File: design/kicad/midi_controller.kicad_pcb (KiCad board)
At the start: 2 copper layers, 166 x 166 mm, 26 parts, among them J1 Conn_01x02_Socket, J2 Conn_01x02_Socket, J3 Conn_01x02_Socket, J4 Conn_01x02_Socket, J5 Conn_01x02_Socket, J6 Conn_01x02_Socket, J7 Conn_01x05, SW1 MIDI_Switch_Pushbutton_PV0H24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, SW2 MIDI_Switch_Pushbutton_PV0H24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, SW3 MIDI_Switch_Pushbutton_PV0H24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, SW4 MIDI_Switch_Pushbutton_PV0H24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, SW5 MIDI_Switch_Pushbutton_PV0H24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, SW6 MIDI_Switch_Pushbutton_PV0H24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, U1 CD74HC4067M

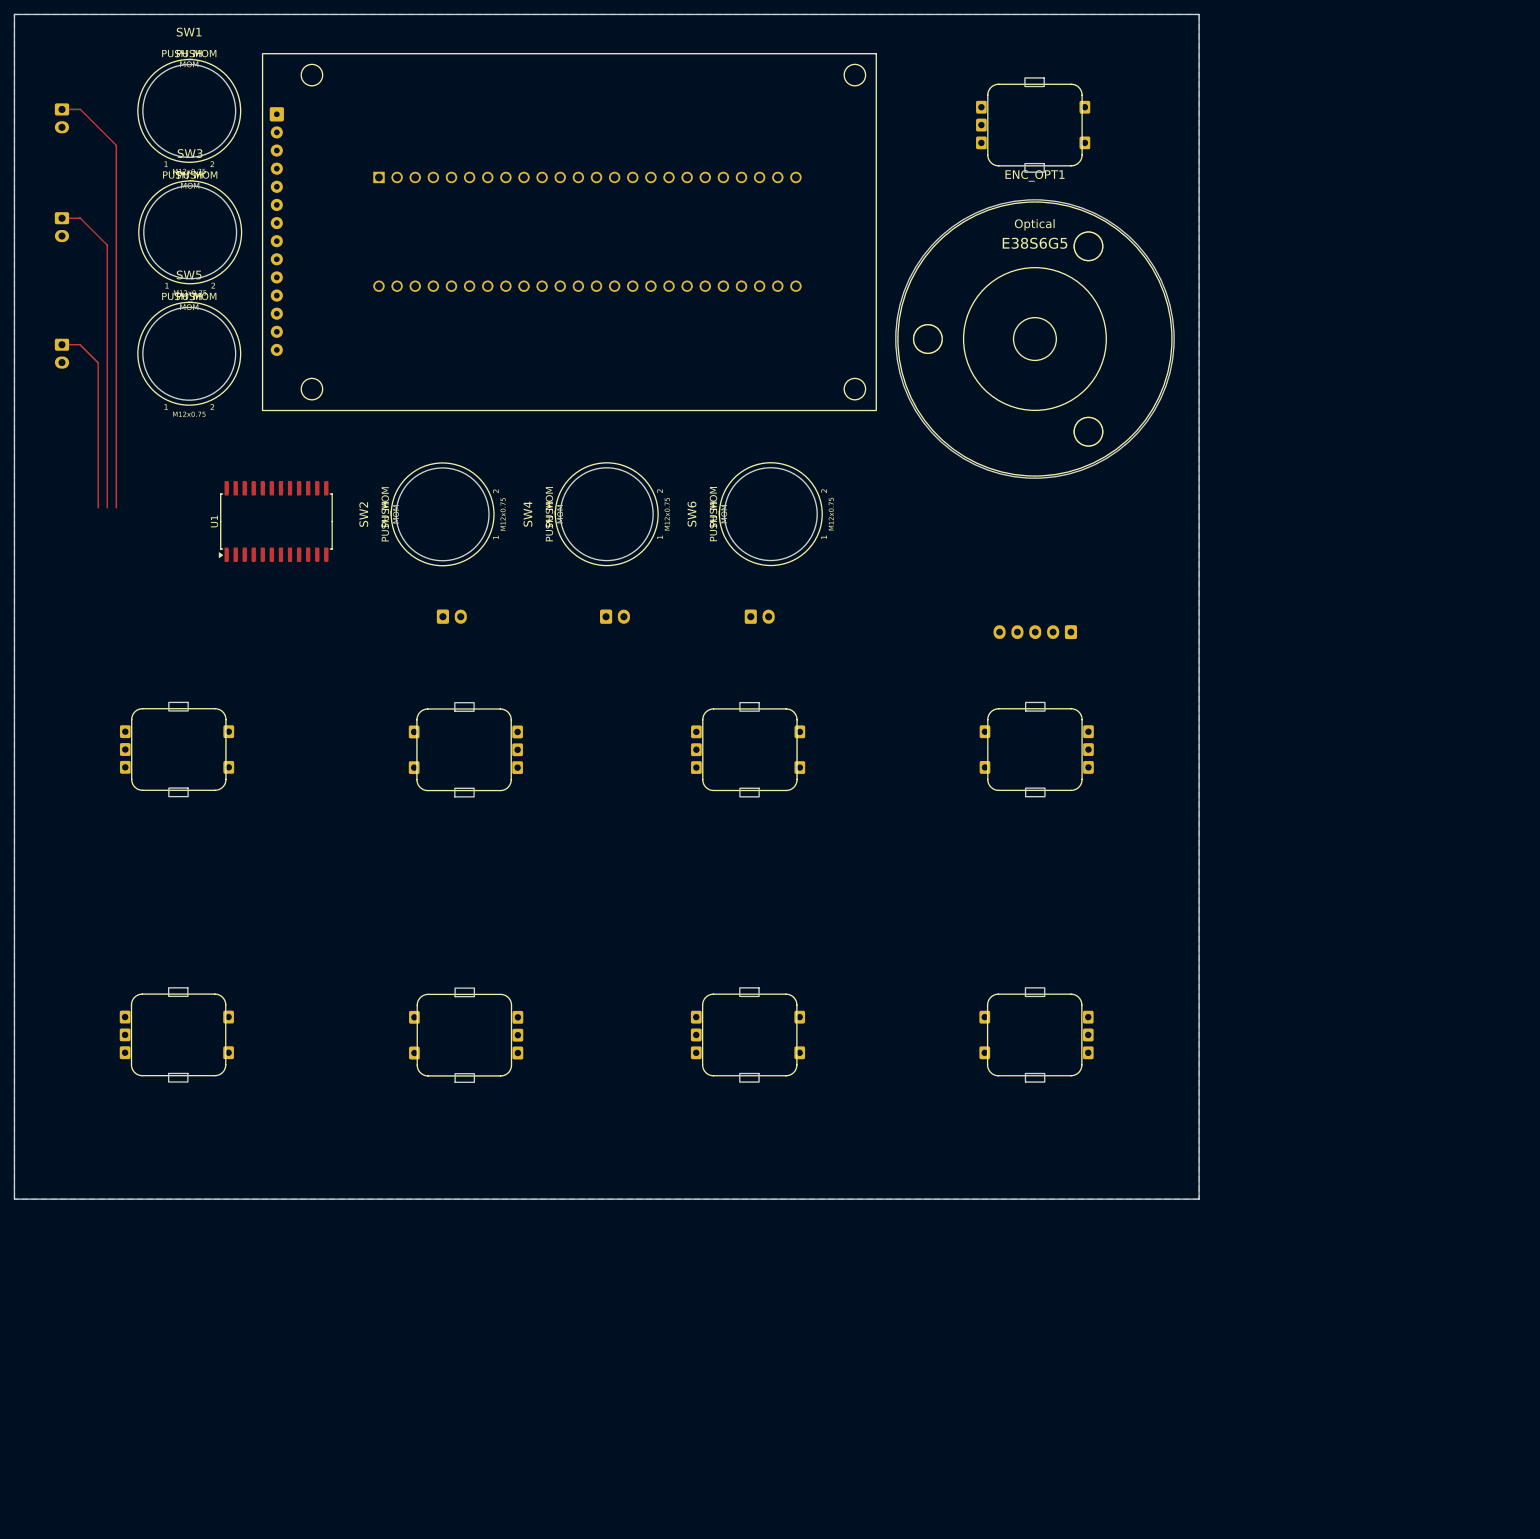
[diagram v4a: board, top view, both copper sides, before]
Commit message: Update kicad binary files
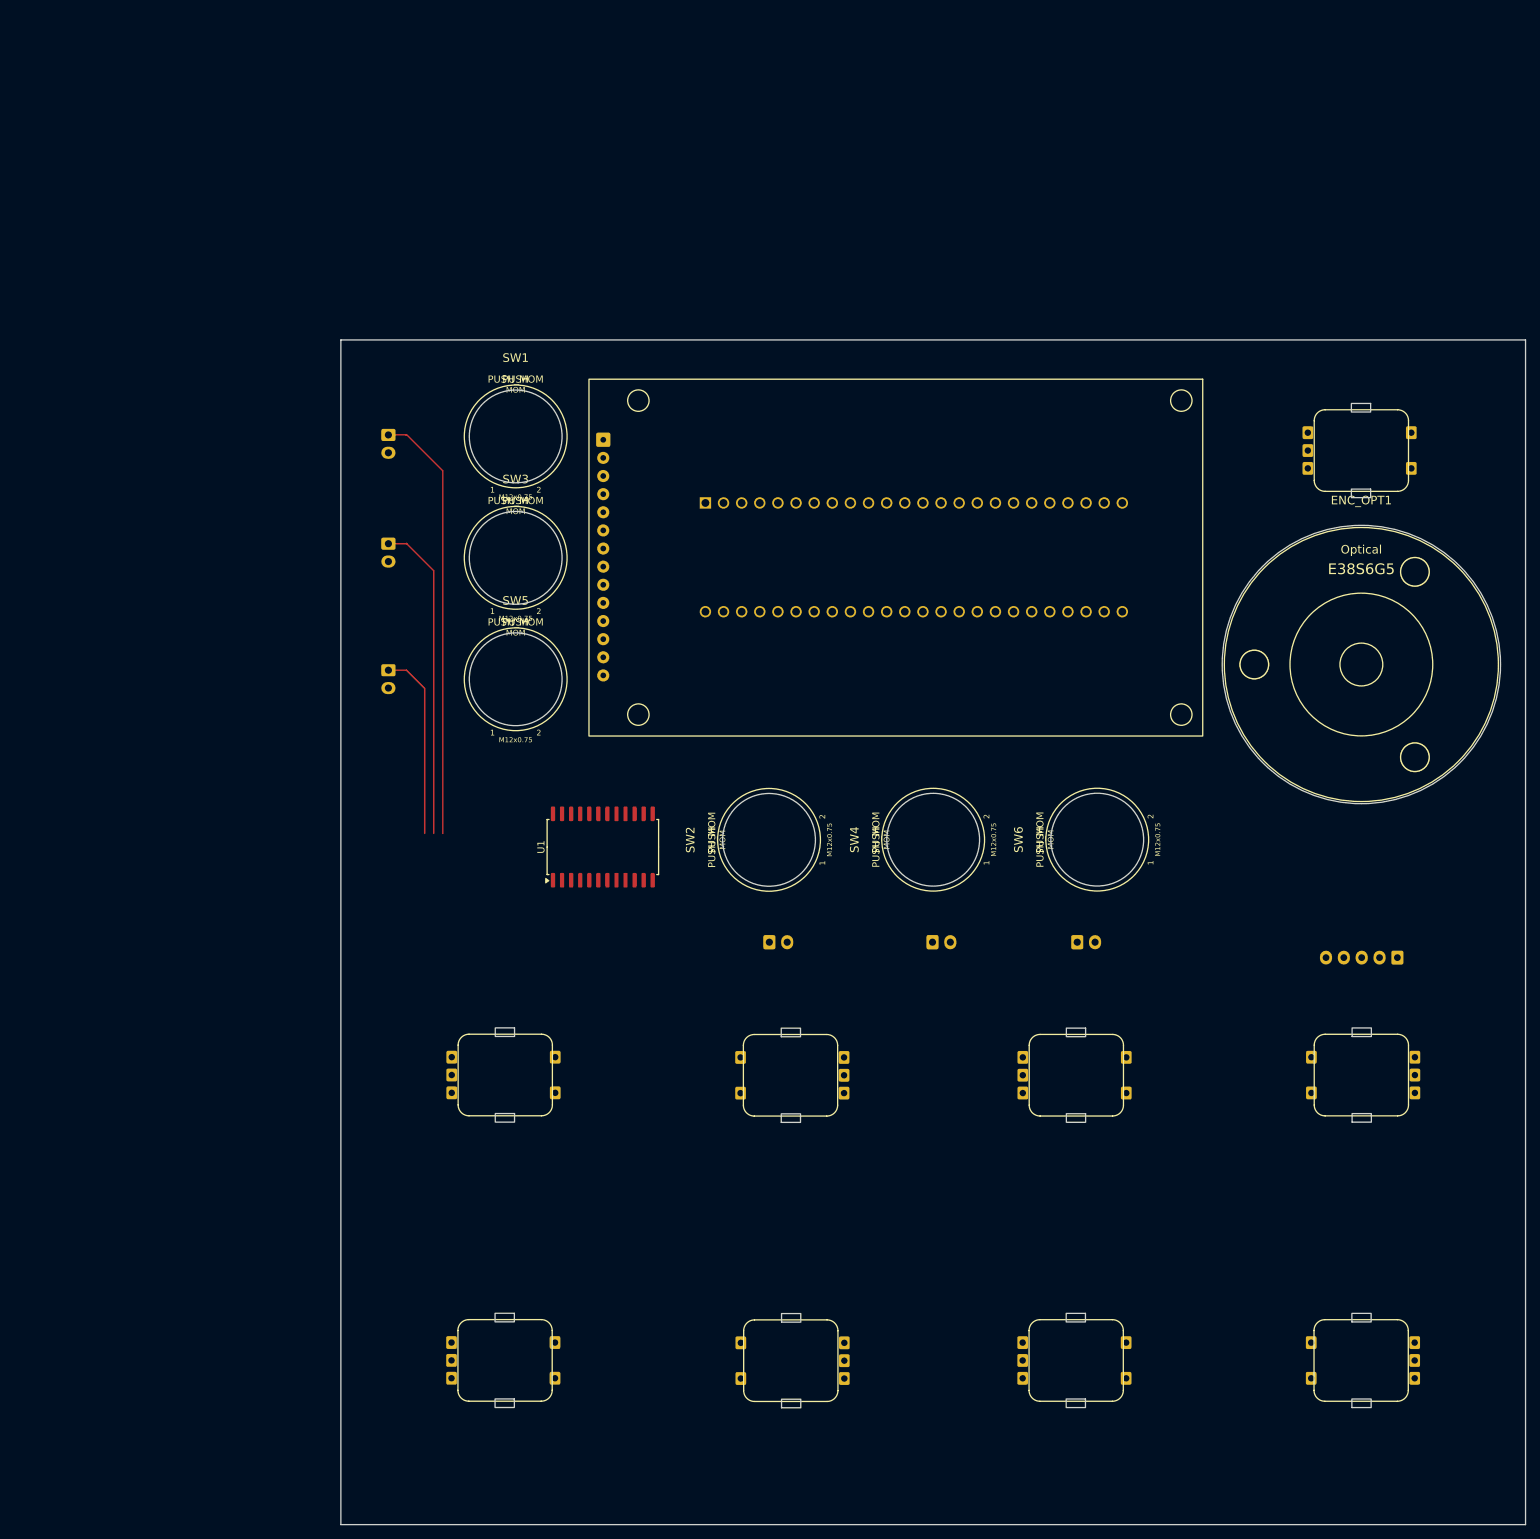
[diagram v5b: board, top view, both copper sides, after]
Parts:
- moved ENC_MECH1 64.6 mm to (100.0, 180.0)
- moved ENC_MECH3 64.6 mm to (180.1, 180.0)
- moved ENC_MECH6 64.6 mm to (140.1, 220.0)
- moved ENC_MECH8 64.6 mm to (220.0, 220.0)
- moved J2 64.6 mm to (83.7, 105.6)
- moved J4 64.6 mm to (180.2, 161.4)
- moved J5 64.6 mm to (159.9, 161.4)
- moved J6 64.6 mm to (137.0, 161.4)
- moved J7 64.6 mm to (225.0, 163.6)
- moved MCU1 64.6 mm to (157.3, 107.5)
- moved D1 64.6 mm to (113.8, 107.5)
- moved ENC_MECH4 64.6 mm to (220.0, 180.0)
- moved ENC_MECH5 64.6 mm to (100.0, 220.0)
- moved ENC_MECH7 64.6 mm to (180.0, 220.0)
- moved ENC_MECH9 64.6 mm to (220.0, 92.5)
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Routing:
- added copper zone on In1.Cu, net /Buttons_Momentary/GND
- removed copper zone on B.Cu, net /Buttons_Momentary/GND
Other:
- copper layers 2 -> 4
- board text removed: "-"
- board text removed: "----"
- board text removed: "1"
- board text removed: "1 of 1"
- board text removed: "10"
- board text removed: "1:1"
- board text removed: "2"
- board text removed: "2025-07-25"
- board text removed: "3"
- board text removed: "4"
- board text removed: "5"
- board text removed: "6"
- board text removed: "7"
- board text removed: "8"
- board text removed: "9"
- board text removed: "A"
- board text removed: "APPROVED"
- board text removed: "B"
- board text removed: "BODY"
- board text removed: "BREAK ALL SHARP EDGES AND REMOVE BURRS"
- board text removed: "C"
- board text removed: "CHECKED"
- board text removed: "D"
- board text removed: "DATE"
- board text removed: "DO NOT SCALE DRAWING"
- board text removed: "DRAWN"
- board text removed: "DWG NO."
- board text removed: "Description"
- board text removed: "ENCODER_OPTICAL_E38S6G5"
- board text removed: "FINISH"
- board text removed: "FIRST ANGLE PROJECTION"
- board text removed: "Item"
- board text removed: "KNOB"
- board text removed: "MATERIAL"
- board text removed: "NAME"
- board text removed: "Name"
- board text removed: "PEC11R_4220F_S0024"
- board text removed: "PLATE_BOTTOM"
- board text removed: "PLATE_FRONT_METAL"
- board text removed: "PUSH_BUTTON"
- board text removed: "Part number"
- board text removed: "Quantity"
- board text removed: "REV."
- board text removed: "SCALE"
- board text removed: "SCREEN"
- board text removed: "SHEET"
- board text removed: "SIGNATURE"
- board text removed: "SIMON BRUN"
- board text removed: "SIZE"
- board text removed: "SURFACE FINISH"
- board text removed: "TITLE"
- board text removed: "UNLESS OTHERWISE SPECIFIED, DIMENSIONS ARE IN MILLIMETERS"
- board text removed: "WEIGHT"

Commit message: Fix hardware pin configuration and rotary encoder parameters
- Updated CS_PIN from 30 to 28 in SystemConstants.hpp to reflect the correct hardware setup for ILI9341.
- Modified rotary encoder parameters in ConfigurationFactory.cpp, changing the first parameter of asRotaryEncoder from 28 to 23 for proper functionality.
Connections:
- net Net-(J7-Pin_2) renamed ENC_A_NAV
- net Net-(J7-Pin_3) renamed ENC_B_NAV
- D1 pad 1: Net-(D1-VCC) -> +5V
- D1 pad 10: Net-(D1-T_CLK) -> unconnected-(D1-T_CLK-Pad10)
- D1 pad 11: Net-(D1-T_CS) -> unconnected-(D1-T_CS-Pad11)
- D1 pad 12: Net-(D1-T_DIN) -> unconnected-(D1-T_DIN-Pad12)
- D1 pad 13: Net-(D1-T_DO) -> unconnected-(D1-T_DO-Pad13)
- D1 pad 14: Net-(D1-T_IRQ) -> unconnected-(D1-T_IRQ-Pad14)
- D1 pad 2: /Buttons_Momentary/GND -> GND
- D1 pad 8: Net-(D1-LED) -> +3V3
- ENC_MECH1 pad 2: /Buttons_Momentary/GND -> GND
- ENC_MECH1 pad A: /MIDI_Encoder_Matrix_2x4_with_push_buttons/1x1.QUAD_A -> /MIDI_Encoder_Matrix_2x4_with_push_buttons/1x1.QUAD_B
- ENC_MECH1 pad B: /MIDI_Encoder_Matrix_2x4_with_push_buttons/1x1.QUAD_A -> /MIDI_Encoder_Matrix_2x4_with_push_buttons/1x1.QUAD_B
- ENC_MECH1 pad C: /Buttons_Momentary/GND -> GND
- ENC_MECH2 pad 2: /Buttons_Momentary/GND -> GND
- ENC_MECH2 pad A: /MIDI_Encoder_Matrix_2x4_with_push_buttons/1x2.QUAD_A -> /MIDI_Encoder_Matrix_2x4_with_push_buttons/1x2.QUAD_B
- ENC_MECH2 pad B: /MIDI_Encoder_Matrix_2x4_with_push_buttons/1x2.QUAD_A -> /MIDI_Encoder_Matrix_2x4_with_push_buttons/1x2.QUAD_B
- ENC_MECH2 pad C: /Buttons_Momentary/GND -> GND
- ENC_MECH3 pad 2: /Buttons_Momentary/GND -> GND
- ENC_MECH3 pad A: /MIDI_Encoder_Matrix_2x4_with_push_buttons/1x3.QUAD_A -> /MIDI_Encoder_Matrix_2x4_with_push_buttons/1x3.QUAD_B
- ENC_MECH3 pad B: /MIDI_Encoder_Matrix_2x4_with_push_buttons/1x3.QUAD_A -> /MIDI_Encoder_Matrix_2x4_with_push_buttons/1x3.QUAD_B
- ENC_MECH3 pad C: /Buttons_Momentary/GND -> GND
- ENC_MECH4 pad 2: /Buttons_Momentary/GND -> GND
- ENC_MECH4 pad A: /MIDI_Encoder_Matrix_2x4_with_push_buttons/1x4.QUAD_A -> /MIDI_Encoder_Matrix_2x4_with_push_buttons/1x4.QUAD_B
- ENC_MECH4 pad B: /MIDI_Encoder_Matrix_2x4_with_push_buttons/1x4.QUAD_A -> /MIDI_Encoder_Matrix_2x4_with_push_buttons/1x4.QUAD_B
- ENC_MECH4 pad C: /Buttons_Momentary/GND -> GND
- ENC_MECH5 pad 2: /Buttons_Momentary/GND -> GND
- ENC_MECH5 pad A: /MIDI_Encoder_Matrix_2x4_with_push_buttons/2x1.QUAD_A -> /MIDI_Encoder_Matrix_2x4_with_push_buttons/2x1.QUAD_B
- ENC_MECH5 pad B: /MIDI_Encoder_Matrix_2x4_with_push_buttons/2x1.QUAD_A -> /MIDI_Encoder_Matrix_2x4_with_push_buttons/2x1.QUAD_B
- ENC_MECH5 pad C: /Buttons_Momentary/GND -> GND
- ENC_MECH6 pad 2: /Buttons_Momentary/GND -> GND
- ENC_MECH6 pad A: /MIDI_Encoder_Matrix_2x4_with_push_buttons/2x2.QUAD_A -> /MIDI_Encoder_Matrix_2x4_with_push_buttons/2x2.QUAD_B
- ENC_MECH6 pad B: /MIDI_Encoder_Matrix_2x4_with_push_buttons/2x2.QUAD_A -> /MIDI_Encoder_Matrix_2x4_with_push_buttons/2x2.QUAD_B
- ENC_MECH6 pad C: /Buttons_Momentary/GND -> GND
- ENC_MECH7 pad 2: /Buttons_Momentary/GND -> GND
- ENC_MECH7 pad A: /MIDI_Encoder_Matrix_2x4_with_push_buttons/2x3.QUAD_A -> /MIDI_Encoder_Matrix_2x4_with_push_buttons/2x3.QUAD_B
- ENC_MECH7 pad B: /MIDI_Encoder_Matrix_2x4_with_push_buttons/2x3.QUAD_A -> /MIDI_Encoder_Matrix_2x4_with_push_buttons/2x3.QUAD_B
- ENC_MECH7 pad C: /Buttons_Momentary/GND -> GND
- ENC_MECH8 pad 2: /Buttons_Momentary/GND -> GND
- ENC_MECH8 pad A: /MIDI_Encoder_Matrix_2x4_with_push_buttons/2x4.QUAD_A -> /MIDI_Encoder_Matrix_2x4_with_push_buttons/2x4.QUAD_B
- ENC_MECH8 pad B: /MIDI_Encoder_Matrix_2x4_with_push_buttons/2x4.QUAD_A -> /MIDI_Encoder_Matrix_2x4_with_push_buttons/2x4.QUAD_B
- ENC_MECH8 pad C: /Buttons_Momentary/GND -> GND
- ENC_MECH9 pad 2: /Buttons_Momentary/GND -> GND
- ENC_MECH9 pad C: /Buttons_Momentary/GND -> GND
- J1 pad 2: /Buttons_Momentary/GND -> GND
- J2 pad 2: /Buttons_Momentary/GND -> GND
- J3 pad 2: /Buttons_Momentary/GND -> GND
- J4 pad 2: /Buttons_Momentary/GND -> GND
- J5 pad 2: /Buttons_Momentary/GND -> GND
- J6 pad 2: /Buttons_Momentary/GND -> GND
- J7 pad 1: Net-(J7-Pin_1) -> +5V
- J7 pad 4: /Buttons_Momentary/GND -> GND
- J7 pad 5: /Buttons_Momentary/GND -> GND
- MCU1 pad 1: /Buttons_Momentary/GND -> GND
- MCU1 pad 10: Net-(D1-LED) -> unconnected-(MCU1-8_TX2_IN1-Pad10)
- MCU1 pad 11: Net-(D1-RST) -> unconnected-(MCU1-9_OUT1C-Pad11)
- MCU1 pad 12: Net-(D1-CS) -> unconnected-(MCU1-10_CS_MQSR-Pad12)
- MCU1 pad 13: Net-(D1-SDI/MOSI) -> unconnected-(MCU1-11_MOSI_CTX1-Pad13)
- MCU1 pad 14: Net-(D1-SDO/MISO) -> unconnected-(MCU1-12_MISO_MQSL-Pad14)
- MCU1 pad 15: Net-(D1-VCC) -> +3V3
- MCU1 pad 16: Net-(D1-T_IRQ) -> unconnected-(MCU1-24_A10_TX6_SCL2-Pad16)
- MCU1 pad 18: Net-(D1-T_DIN) -> Net-(D1-SDI/MOSI)
- MCU1 pad 19: Net-(D1-T_CLK) -> Net-(D1-SCK)
- MCU1 pad 2: unconnected-(MCU1-0_RX1_CRX2_CS1-Pad2) -> Net-(D1-DC)
- MCU1 pad 20: Net-(D1-T_CS) -> Net-(D1-CS)
- MCU1 pad 21: /Encoder with Push Button_Navigation/QUAD_A -> Net-(D1-RST)
- MCU1 pad 22: /Encoder with Push Button_Navigation/QUAD_B -> unconnected-(MCU1-30_CRX3-Pad22)
- MCU1 pad 27: /MIDI_Encoder_Matrix_2x4_with_push_buttons/1x1.QUAD_A -> unconnected-(MCU1-35_TX8-Pad27)
- MCU1 pad 28: /MIDI_Encoder_Matrix_2x4_with_push_buttons/1x1.QUAD_A -> /MIDI_Encoder_Matrix_2x4_with_push_buttons/2x4.QUAD_B
- MCU1 pad 29: Net-(D1-DC) -> /MIDI_Encoder_Matrix_2x4_with_push_buttons/2x4.QUAD_B
- MCU1 pad 3: Net-(D1-T_DO) -> Net-(D1-SDO/MISO)
- MCU1 pad 30: /MIDI_Encoder_Matrix_2x4_with_push_buttons/1x2.QUAD_A -> /MIDI_Encoder_Matrix_2x4_with_push_buttons/2x3.QUAD_B
- MCU1 pad 31: /MIDI_Encoder_Matrix_2x4_with_push_buttons/1x2.QUAD_A -> /MIDI_Encoder_Matrix_2x4_with_push_buttons/2x3.QUAD_B
- MCU1 pad 32: /MIDI_Encoder_Matrix_2x4_with_push_buttons/1x3.QUAD_A -> /MIDI_Encoder_Matrix_2x4_with_push_buttons/2x2.QUAD_B
- MCU1 pad 33: /MIDI_Encoder_Matrix_2x4_with_push_buttons/1x3.QUAD_A -> /MIDI_Encoder_Matrix_2x4_with_push_buttons/2x2.QUAD_B
- MCU1 pad 34: unconnected-(MCU1-GND-Pad34) -> GND
- MCU1 pad 35: Net-(D1-SCK) -> unconnected-(MCU1-13_SCK_LED-Pad35)
- MCU1 pad 36: /MIDI_Encoder_Matrix_2x4_with_push_buttons/1x4.QUAD_A -> /MIDI_Encoder_Matrix_2x4_with_push_buttons/2x1.QUAD_B
- MCU1 pad 37: /MIDI_Encoder_Matrix_2x4_with_push_buttons/1x4.QUAD_A -> /MIDI_Encoder_Matrix_2x4_with_push_buttons/2x1.QUAD_B
- MCU1 pad 38: /MIDI_Encoder_Matrix_2x4_with_push_buttons/2x1.QUAD_A -> /MIDI_Encoder_Matrix_2x4_with_push_buttons/1x4.QUAD_B
- MCU1 pad 39: /MIDI_Encoder_Matrix_2x4_with_push_buttons/2x1.QUAD_A -> /MIDI_Encoder_Matrix_2x4_with_push_buttons/1x4.QUAD_B
- MCU1 pad 4: unconnected-(MCU1-2_OUT2-Pad4) -> COM
- MCU1 pad 40: /MIDI_Encoder_Matrix_2x4_with_push_buttons/2x2.QUAD_A -> /MIDI_Encoder_Matrix_2x4_with_push_buttons/1x3.QUAD_B
- MCU1 pad 41: /MIDI_Encoder_Matrix_2x4_with_push_buttons/2x2.QUAD_A -> /MIDI_Encoder_Matrix_2x4_with_push_buttons/1x3.QUAD_B
- MCU1 pad 42: /MIDI_Encoder_Matrix_2x4_with_push_buttons/2x3.QUAD_A -> /MIDI_Encoder_Matrix_2x4_with_push_buttons/1x2.QUAD_B
- MCU1 pad 43: /MIDI_Encoder_Matrix_2x4_with_push_buttons/2x3.QUAD_A -> /MIDI_Encoder_Matrix_2x4_with_push_buttons/1x2.QUAD_B
- MCU1 pad 44: /MIDI_Encoder_Matrix_2x4_with_push_buttons/2x4.QUAD_A -> /MIDI_Encoder_Matrix_2x4_with_push_buttons/1x1.QUAD_B
- MCU1 pad 45: /MIDI_Encoder_Matrix_2x4_with_push_buttons/2x4.QUAD_A -> /MIDI_Encoder_Matrix_2x4_with_push_buttons/1x1.QUAD_B
- MCU1 pad 46: unconnected-(MCU1-3V3-Pad46) -> +3V3
- MCU1 pad 47: unconnected-(MCU1-GND-Pad47) -> GND
- MCU1 pad 48: Net-(J7-Pin_1) -> +5V
- MCU1 pad 5: Net-(MCU1-3_LRCLK2) -> S0
- MCU1 pad 6: Net-(MCU1-4_BCLK2) -> S1
- MCU1 pad 7: Net-(MCU1-5_IN2) -> S2
- MCU1 pad 8: Net-(MCU1-6_OUT1D) -> S3
- MCU1 pad 9: Net-(MCU1-7_RX2_OUT1A) -> unconnected-(MCU1-7_RX2_OUT1A-Pad9)
- U1 pad 1: Net-(MCU1-7_RX2_OUT1A) -> COM
- U1 pad 10: Net-(MCU1-6_OUT1D) -> S0
- U1 pad 11: Net-(MCU1-5_IN2) -> S1
- U1 pad 12: /Buttons_Momentary/GND -> GND
- U1 pad 13: Net-(MCU1-3_LRCLK2) -> S3
- U1 pad 14: Net-(MCU1-4_BCLK2) -> S2
- U1 pad 15: /Buttons_Momentary/GND -> GND
- U1 pad 24: Net-(D1-VCC) -> +3V3
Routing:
- added copper zone on In1.Cu, net GND
- removed copper zone on In1.Cu, net /Buttons_Momentary/GND
